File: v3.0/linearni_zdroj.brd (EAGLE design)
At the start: 160 x 100 mm, 29 parts, among them IC1 LM358N, IC2 LM358N, Q1 TIP120, Q2 TIP120

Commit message: zpřehlednění schématu
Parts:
- removed C1: 470u, rcl:E3,5-8
- removed R3: (no value), rcl:R0805
- removed ZD2: (no value), devices:DO34-5
- added ZD1, ZD3, ZD4: (no value), devices:MINIMELF
- moved R1 258.6 mm to (45.7, 57.1)
- moved R7 248.3 mm to (34.3, 30.5)
- moved R2 236.4 mm to (63.5, 36.8)
- moved C9 189.5 mm to (21.6, 55.9)
- moved C8 185.7 mm to (16.5, 58.4)
- moved R10 75.9 mm to (12.7, 53.3)
- moved IC2 75.5 mm to (11.4, 33.0)
- moved U$5 74.1 mm to (19.1, 43.2)
- moved R9 65.7 mm to (36.8, 41.9)
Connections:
- net A1: now also ZD1.C
- net A3: now also ZD4.C; no longer ZD2.C
- net GND: now also ZD1.A, ZD3.A, ZD4.A; no longer C1.-, R3.1, ZD2.A
- net N$11: now also ZD3.C
- net N$13: no longer C1.+, R3.2

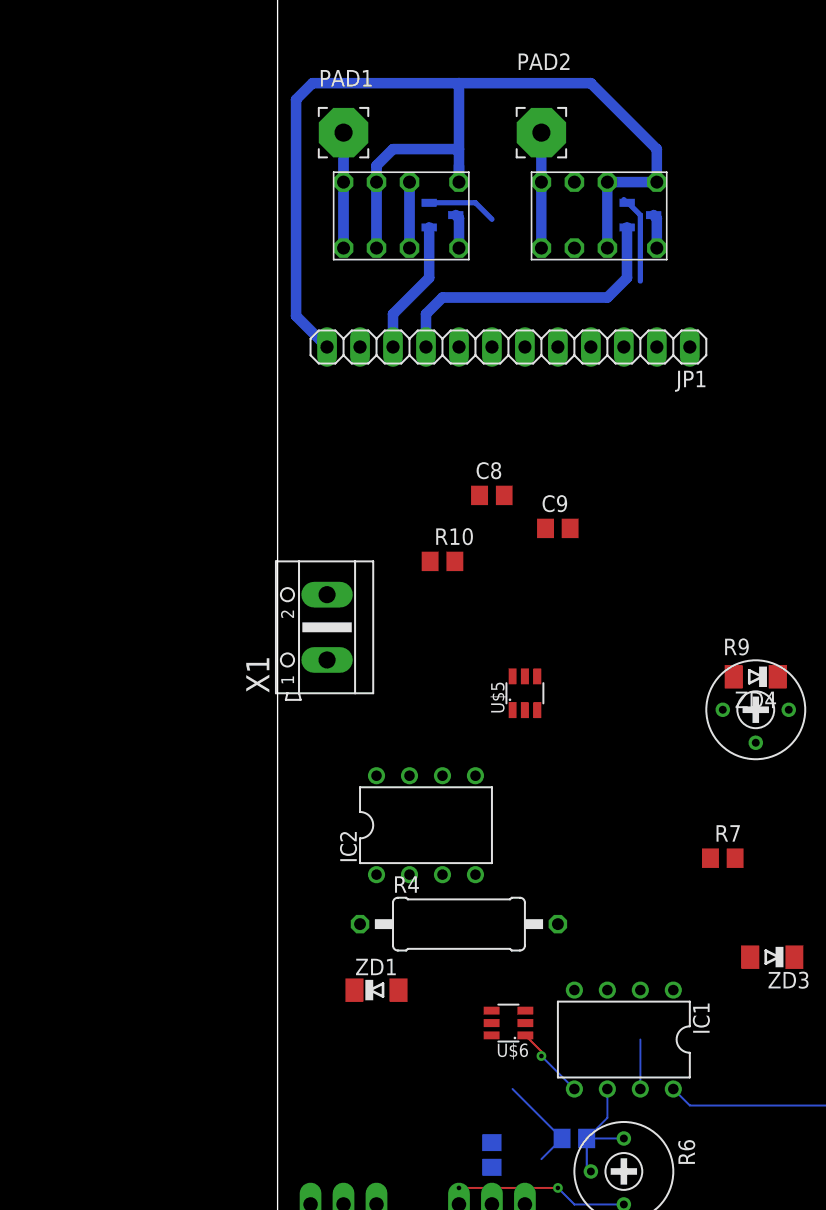
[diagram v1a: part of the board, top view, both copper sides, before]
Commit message: přidány pull-up rezistory I2C
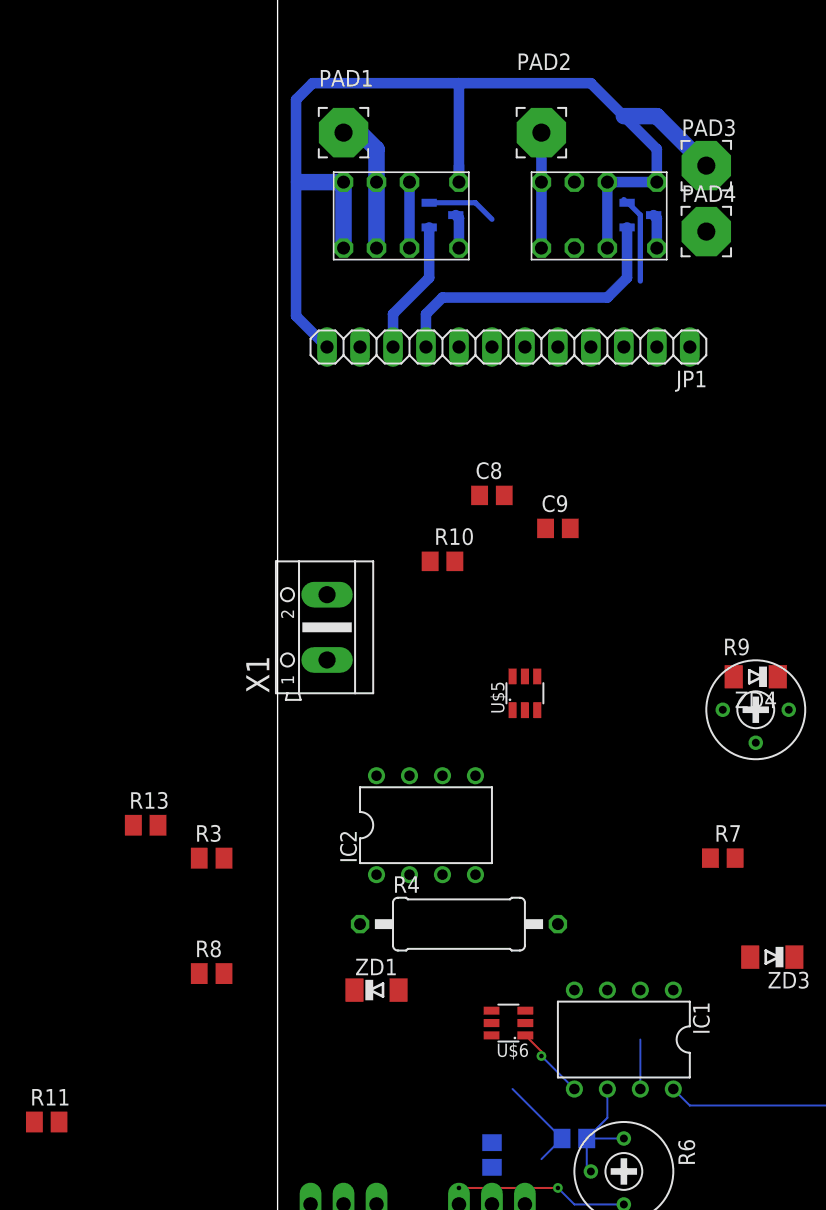
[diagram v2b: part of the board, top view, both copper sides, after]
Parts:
- added PAD3, PAD4: (no value), wirepad:3,81/1,4
- added R11, R13, R3, R8: (no value), rcl_my:M0805
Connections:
- net +24V: now also PAD3.1, U$2.8, U$2.9; no longer U$2.11, U$2.6
- net +3V3: now also R11.2, R13.2, R3.2, R8.2
- net GND: now also PAD4.1
- net N$10: now also U$2.11, U$2.6; no longer U$2.8, U$2.9
- net SCL: now also R13.1
- net SCL2: now also R8.1
- net SDA: now also R3.1
- net SDA2: now also R11.1
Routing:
- net +24V: track 84.0 -> 87.2 mm
- net N$10: track 8.89 -> 10.7 mm
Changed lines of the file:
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@@
 <attribute name="VALUE" x="38.481" y="46.863" size="1.27" layer="27" rot="R180"/>
+</element>
+<element name="PAD3" library="wirepad" library_urn="urn:adsk.eagle:library:412" package="3,81/1,4" package3d_urn="urn:adsk.eagle:package:30835/1" value="" x="33.02" y="83.82" smashed="yes">
+<attribute name="NAME" x="31.115" y="86.106" size="1.27" layer="25" ratio="10"/>
+<attribute name="POPULARITY" value="14" x="33.02" y="83.82" size="1.778" layer="27" display="off"/>
+<attribute name="VALUE" x="33.02" y="85.02" size="0.0254" layer="27"/>
+</element>
+<element name="PAD4" library="wirepad" library_urn="urn:adsk.eagle:library:412" package="3,81/1,4" package3d_urn="urn:adsk.eagle:package:30835/1" value="" x="33.02" y="78.74" smashed="yes">
+<attribute name="NAME" x="31.115" y="81.026" size="1.27" layer="25" ratio="10"/>
+<attribute name="POPULARITY" value="14" x="33.02" y="78.74" size="1.778" layer="27" display="off"/>
+<attribute name="VALUE" x="33.02" y="79.94" size="0.0254" layer="27"/>
+</element>
+<element name="R3" library="rcl_my" package="M0805" value="" x="-5.08" y="30.48" smashed="yes">
+<attribute name="NAME" x="-6.35" y="31.75" size="1.27" layer="25"/>
+<attribute name="VALUE" x="-6.35" y="27.94" size="1.27" layer="27"/>
+</element>
+<element name="R8" library="rcl_my" package="M0805" value="" x="-5.08" y="21.59" smashed="yes">
+<attribute name="NAME" x="-6.35" y="22.86" size="1.27" layer="25"/>
+<attribute name="VALUE" x="-6.35" y="19.05" size="1.27" layer="27"/>
+</element>
+<element name="R11" library="rcl_my" package="M0805" value="" x="-17.78" y="10.16" smashed="yes">
+<attribute name="NAME" x="-19.05" y="11.43" size="1.27" layer="25"/>
+<attribute name="VALUE" x="-19.05" y="7.62" size="1.27" layer="27"/>
+</element>
+<element name="R13" library="rcl_my" package="M0805" value="" x="-10.16" y="33.02" smashed="yes">
+<attribute name="NAME" x="-11.43" y="34.29" size="1.27" layer="25"/>
+<attribute name="VALUE" x="-11.43" y="30.48" size="1.27" layer="27"/>
 </element>
 </elements>
@@
 <contactref element="ZD1" pad="A"/>
 <contactref element="ZD3" pad="A"/>
+<contactref element="PAD4" pad="1"/>
 <wire x1="16.51" y1="79.69" x2="26.67" y2="81.2053" width="0" layer="19" extent="16-16"/>
 <wire x1="6.35" y1="69.85" x2="11.6753" y2="80.96" width="0" layer="19" extent="16-16"/>
@@
 <wire x1="35.13" y1="44.45" x2="19.05" y2="41.88" width="0" layer="19" extent="1-1"/>
 <wire x1="44.77" y1="57.15" x2="35.13" y2="44.45" width="0" layer="19" extent="1-1"/>
+<wire x1="33.02" y1="78.74" x2="20.32" y2="7.3" width="0" layer="19" extent="16-16"/>
 </signal>
 <signal name="VCC/2">
@@
 <contactref element="U$5" pad="5"/>
 <contactref element="JP1" pad="8"/>
+<contactref element="R13" pad="1"/>
 <wire x1="19.05" y1="44.48" x2="13.97" y2="69.85" width="0" layer="19" extent="1-1"/>
+<wire x1="-11.11" y1="33.02" x2="19.05" y2="44.48" width="0" layer="19" extent="1-1"/>
 </signal>
 <signal name="SDA">
 <contactref element="U$5" pad="4"/>
 <contactref element="JP1" pad="7"/>
+<contactref element="R3" pad="1"/>
 <wire x1="20" y1="44.48" x2="16.51" y2="69.85" width="0" layer="19" extent="1-1"/>
+<wire x1="-6.03" y1="30.48" x2="20" y2="44.48" width="0" layer="19" extent="1-1"/>
 </signal>
 <signal name="N$9">
@@
 <wire x1="5.08" y1="3.81" x2="10.16" y2="77.47" width="0" layer="19" extent="1-1"/>
 </signal>
-<signal name="N$10">
-<contactref element="PAD1" pad="1"/>
-<contactref element="U$2" pad="8"/>
-<wire x1="5.08" y1="86.36" x2="5.08" y2="82.55" width="0.8128" layer="16"/>
-<contactref element="U$2" pad="9"/>
-<wire x1="5.08" y1="77.47" x2="5.08" y2="82.55" width="0.8128" layer="16"/>
-</signal>
 <signal name="+24V">
-<contactref element="U$2" pad="6"/>
 <contactref element="U$1" pad="1"/>
 <contactref element="U$2" pad="1"/>
-<wire x1="7.62" y1="82.55" x2="7.62" y2="83.82" width="0.8128" layer="16"/>
-<wire x1="7.62" y1="83.82" x2="8.89" y2="85.09" width="0.8128" layer="16"/>
-<wire x1="8.89" y1="85.09" x2="13.97" y2="85.09" width="0.8128" layer="16"/>
 <wire x1="13.97" y1="83.82" x2="13.97" y2="82.55" width="0.8128" layer="16"/>
-<contactref element="U$2" pad="11"/>
 <contactref element="U$1" pad="4"/>
 <contactref element="U$1" pad="13"/>
 <wire x1="25.4" y1="77.47" x2="25.4" y2="82.55" width="0.8128" layer="16"/>
-<wire x1="7.62" y1="77.47" x2="7.62" y2="82.55" width="0.8128" layer="16"/>
-<wire x1="29.21" y1="85.09" x2="24.13" y2="90.17" width="0.8128" layer="16"/>
+<wire x1="29.21" y1="85.09" x2="26.67" y2="87.63" width="0.8128" layer="16"/>
+<wire x1="26.67" y1="87.63" x2="24.13" y2="90.17" width="0.8128" layer="16"/>
 <wire x1="24.13" y1="90.17" x2="13.97" y2="90.17" width="0.8128" layer="16"/>
-<wire x1="13.97" y1="85.09" x2="13.97" y2="82.55" width="0.8128" layer="16"/>
 <wire x1="29.21" y1="82.55" x2="29.21" y2="85.09" width="0.8128" layer="16"/>
 <wire x1="25.4" y1="82.55" x2="29.21" y2="82.55" width="0.8128" layer="16"/>
@@
 <wire x1="1.4224" y1="88.9" x2="2.6924" y2="90.17" width="0.8128" layer="16"/>
 <wire x1="2.6924" y1="90.17" x2="13.97" y2="90.17" width="0.8128" layer="16"/>
-<wire x1="13.97" y1="85.09" x2="13.97" y2="90.17" width="0.8128" layer="16"/>
+<wire x1="13.97" y1="82.55" x2="13.97" y2="90.17" width="0.8128" layer="16"/>
+<contactref element="U$2" pad="8"/>
+<contactref element="U$2" pad="9"/>
+<wire x1="5.08" y1="77.47" x2="5.08" y2="82.55" width="1.27" layer="16"/>
+<wire x1="5.08" y1="82.55" x2="1.651" y2="82.55" width="1.27" layer="16"/>
+<contactref element="PAD3" pad="1"/>
+<wire x1="33.02" y1="83.82" x2="29.21" y2="87.63" width="1.27" layer="16"/>
+<wire x1="29.21" y1="87.63" x2="26.67" y2="87.63" width="1.27" layer="16"/>
+<wire x1="3.81" y1="69.85" x2="5.08" y2="77.47" width="0" layer="19" extent="1-1"/>
 </signal>
 <signal name="N$16">
@@
 <contactref element="U$6" pad="6"/>
 <contactref element="JP1" pad="1"/>
-<wire x1="19.08" y1="18.73" x2="31.75" y2="69.85" width="0" layer="19" extent="1-1"/>
+<contactref element="R11" pad="2"/>
+<contactref element="R8" pad="2"/>
+<contactref element="R13" pad="2"/>
+<contactref element="R3" pad="2"/>
+<wire x1="18.1" y1="44.48" x2="31.75" y2="69.85" width="0" layer="19" extent="1-1"/>
+<wire x1="20" y1="41.88" x2="18.1" y2="44.48" width="0" layer="19" extent="1-1"/>
+<wire x1="19.08" y1="18.73" x2="20" y2="41.88" width="0" layer="19" extent="1-1"/>
 <wire x1="16.48" y1="16.83" x2="19.08" y2="18.73" width="0" layer="19" extent="1-1"/>
-<wire x1="18.1" y1="44.48" x2="16.48" y2="16.83" width="0" layer="19" extent="1-1"/>
-<wire x1="20" y1="41.88" x2="18.1" y2="44.48" width="0" layer="19" extent="1-1"/>
+<wire x1="-4.13" y1="30.48" x2="16.48" y2="16.83" width="0" layer="19" extent="1-1"/>
+<wire x1="-4.13" y1="21.59" x2="-4.13" y2="30.48" width="0" layer="19" extent="1-1"/>
+<wire x1="-16.83" y1="10.16" x2="-4.13" y2="21.59" width="0" layer="19" extent="1-1"/>
+<wire x1="-9.21" y1="33.02" x2="-16.83" y2="10.16" width="0" layer="19" extent="1-1"/>
 </signal>
 <signal name="SCL2">
 <contactref element="U$6" pad="5"/>
 <contactref element="JP1" pad="3"/>
+<contactref element="R8" pad="1"/>
 <wire x1="16.48" y1="17.78" x2="26.67" y2="69.85" width="0" layer="19" extent="1-1"/>
+<wire x1="-6.03" y1="21.59" x2="16.48" y2="17.78" width="0" layer="19" extent="1-1"/>
 </signal>
 <signal name="SDA2">
 <contactref element="U$6" pad="4"/>
 <contactref element="JP1" pad="2"/>
+<contactref element="R11" pad="1"/>
 <wire x1="16.48" y1="18.73" x2="29.21" y2="69.85" width="0" layer="19" extent="1-1"/>
+<wire x1="-18.73" y1="10.16" x2="16.48" y2="18.73" width="0" layer="19" extent="1-1"/>
 </signal>
 <signal name="N$14">
@@
 <wire x1="11.6753" y1="75.1753" x2="8.89" y2="72.39" width="0.8128" layer="16"/>
 </signal>
+<signal name="N$10">
+<contactref element="U$2" pad="6"/>
+<contactref element="U$2" pad="11"/>
+<contactref element="PAD1" pad="1"/>
+<wire x1="7.62" y1="77.47" x2="7.62" y2="82.55" width="1.27" layer="16"/>
+<wire x1="5.08" y1="86.36" x2="6.35" y2="86.36" width="1.27" layer="16"/>
+<wire x1="6.35" y1="86.36" x2="7.62" y2="85.09" width="1.27" layer="16"/>
+<wire x1="7.62" y1="85.09" x2="7.62" y2="82.55" width="1.27" layer="16"/>
+</signal>
 </signals>

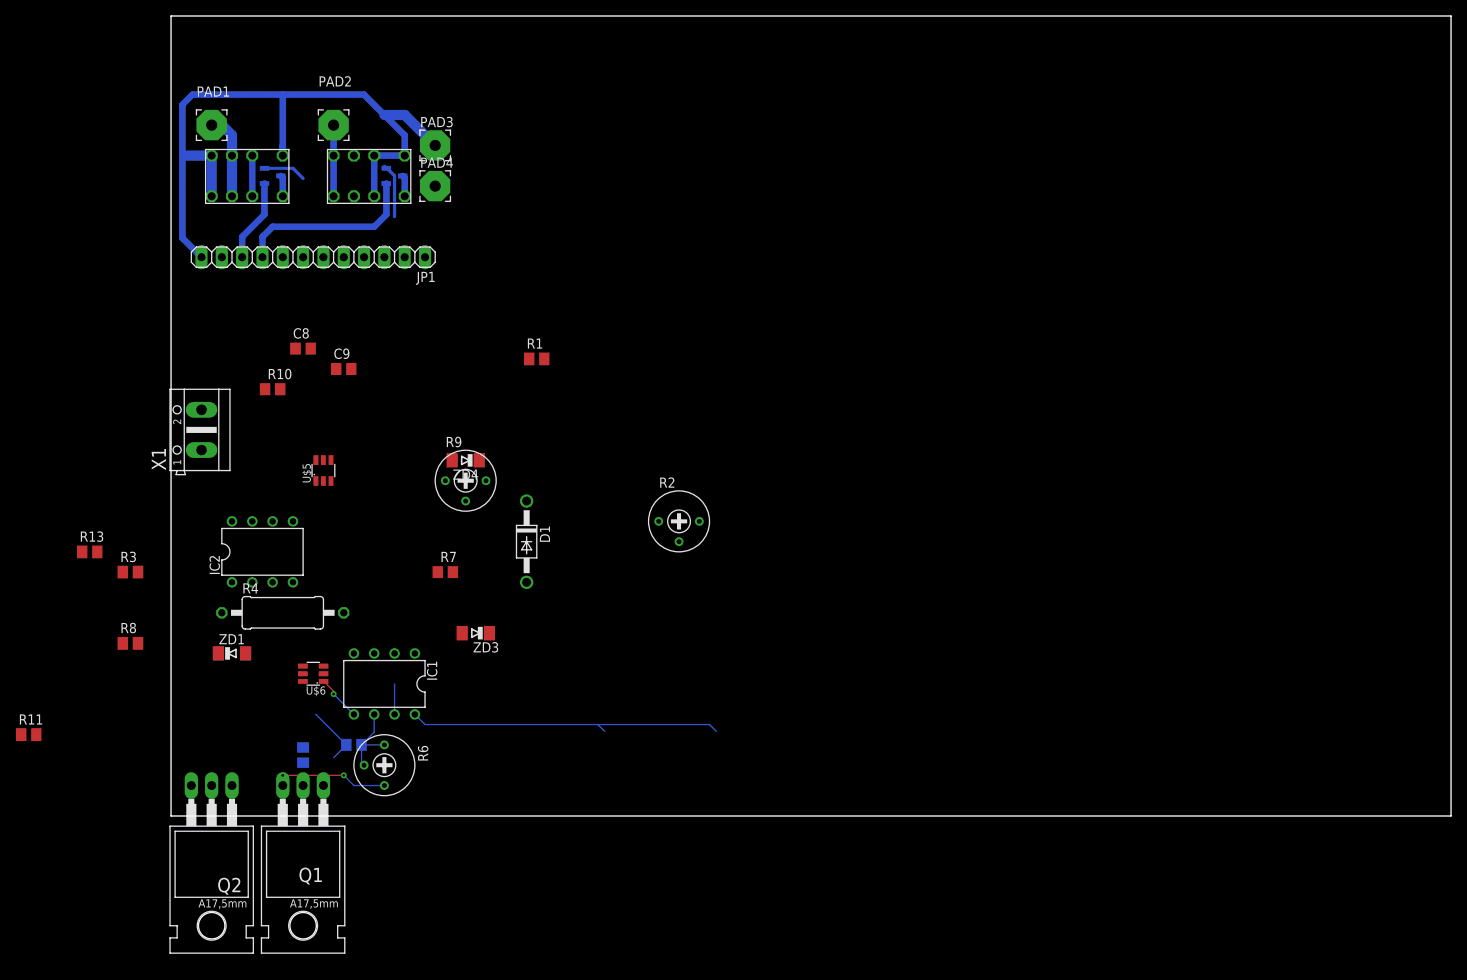
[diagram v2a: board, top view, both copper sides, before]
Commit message: deska lineárního regulátoru
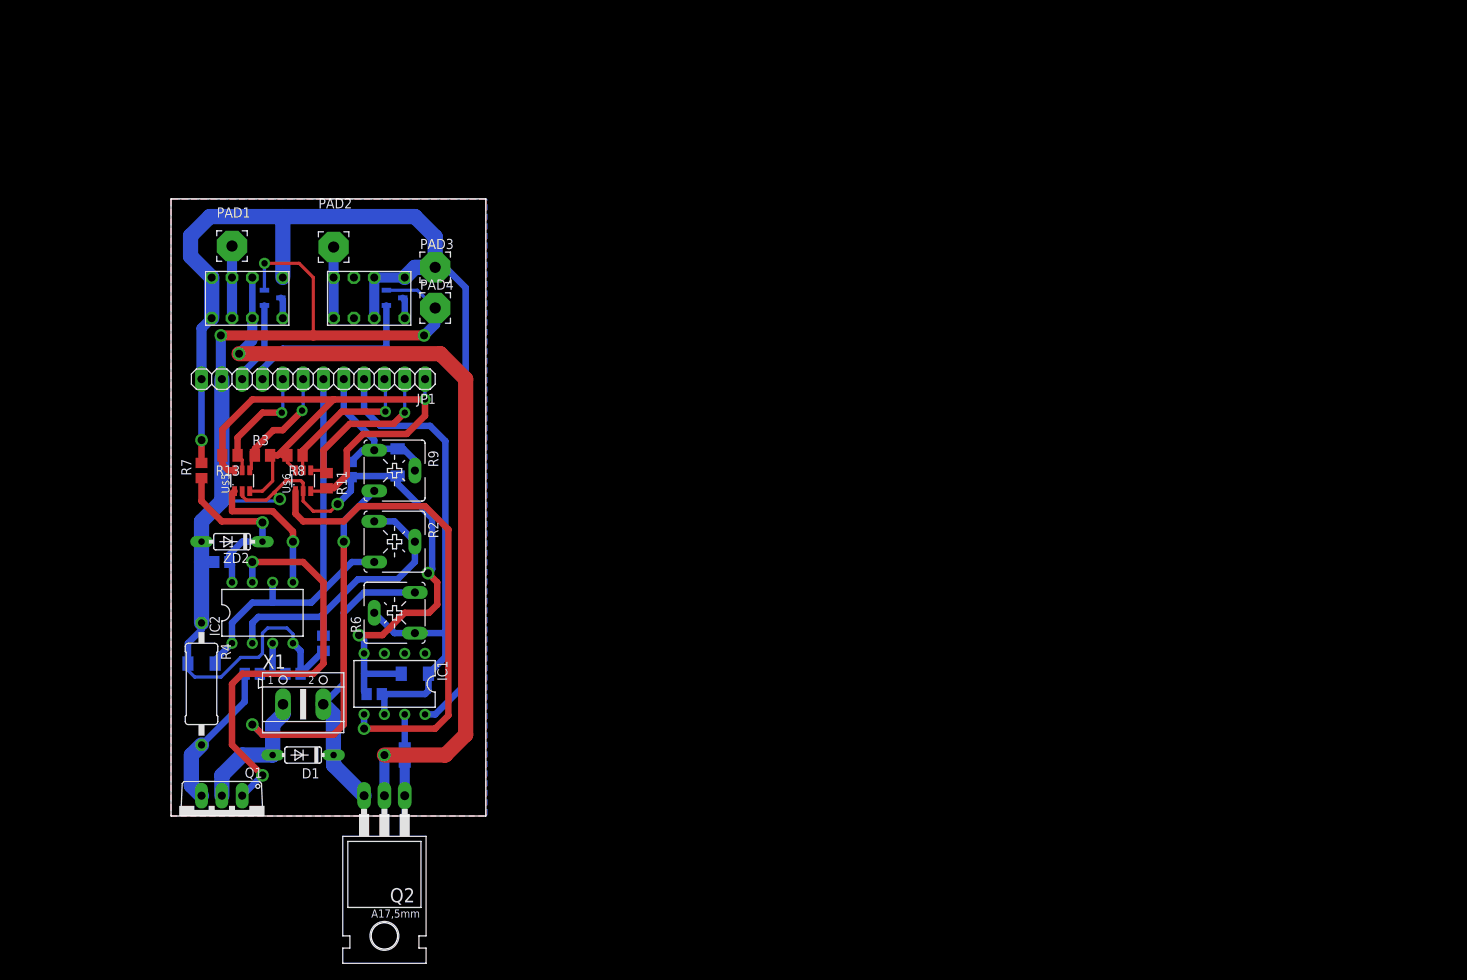
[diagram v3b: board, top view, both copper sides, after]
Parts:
- removed C8: (no value), rcl:C0805
- added C1: (no value), rcl:C0805
- added R14: (no value), rcl:R0805
- added ZD2: (no value), devices:DO35Z7
- D1: value 1N4004 -> (none); device diode:DO41-10 -> devices:DO35-7B
- Q1: value TIP120 -> IRFZ34NAV; device transistor-power:TO220AH -> devices:TO220AV
- R2, R6, R9: device rcl:RTRIM3339P -> pot:CA6V
- moved R11 48.9 mm to (19.4, 41.9), turned to 270 degrees
- moved R1 44.5 mm to (19.1, 21.6), flipped to the bottom, turned to 90 degrees
- moved D1 38.6 mm to (16.5, 7.62), turned to 180 degrees
- moved X1 36.6 mm to (16.5, 14.0), turned to 0 degrees
- moved R2 35.7 mm to (27.9, 34.3), turned to 270 degrees
- moved R7 33.0 mm to (3.81, 43.2), turned to 90 degrees
- moved R8 31.2 mm to (15.5, 45.1), turned to 180 degrees
- moved C9 28.5 mm to (6.35, 31.8), flipped to the bottom
- moved U$6 24.2 mm to (16.5, 41.9), turned to 0 degrees
- moved R3 22.0 mm to (11.4, 45.1)
- moved Q2 21.6 mm to (26.7, -3.81)
- moved R13 21.3 mm to (7.37, 45.1), turned to 180 degrees
- moved R6 19.1 mm to (27.9, 25.4), turned to 90 degrees
- moved PAD1 15.3 mm to (7.62, 71.2)
- moved U$1 15.2 mm to (25.4, 64.8)
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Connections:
- removed net A1: IC1.2, IC2.1, R2.3, ZD1.C
- removed net A3: R10.2, R9.1, R9.2, ZD4.C
- removed net N$11: IC1.6, R5.2, R6.1, R6.2, ZD3.C
- removed net N$14: JP1.4
- removed net N$15: JP1.5
- removed net N$18: JP1.6
- removed net VCC/2: C8.1, C9.1, IC1.8, IC2.8
- new net ADC0: IC2.1, IC2.6, JP1.6, R2.E, ZD1.C
- new net ADC1: JP1.5, R10.2, R9.A, R9.S, ZD4.C
- new net ADC2: IC1.6, JP1.4, R5.2, R6.A, R6.S, ZD3.C
- new net N$20: C1.1, IC2.3, R14.1
- net +24V: now also IC1.8, R7.2
- net GND: now also C1.2, ZD2.A; no longer C8.2
- net N$1: now also Q1.S, R14.2; no longer IC2.3, Q1.E
- net N$13: now also R6.E; no longer R6.3
- net N$2: now also IC2.7, Q1.G; no longer IC1.1, R7.2
- net N$3: now also R2.A, R2.S; no longer R2.1, R2.2
- net N$5: now also C9.1, IC2.8, ZD2.C; no longer Q1.B
- net N$6: now also IC2.5; no longer IC1.3
- net N$7: now also Q1.D, R9.E; no longer Q1.C, R9.3
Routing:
- net GND: track 19.8 -> 206.7 mm, vias 0 -> 7
- net N$8: track 5.08 -> 100.6 mm, vias 0 -> 2
- net +3V3: track 0.00 -> 79.6 mm, vias 0 -> 1
- net ADC2: track 0.00 -> 66.3 mm
- net N$7: track 0.00 -> 63.2 mm, vias 0 -> 2
- net +24V: track 87.2 -> 148.3 mm, vias 0 -> 1
- net ADC0: track 0.00 -> 55.8 mm
- net N$9: track 5.70 -> 60.6 mm
- net N$2: track 0.00 -> 51.7 mm, vias 0 -> 2
- net VCC/2: track 39.8 -> 0.00 mm
- net N$3: track 0.00 -> 37.4 mm
- net N$13: track 13.2 -> 36.0 mm, vias 2 -> 0
- net N$5: track 0.00 -> 22.4 mm, vias 0 -> 1
- net SDA2: track 0.00 -> 21.4 mm, vias 0 -> 1
- net ADC1: track 0.00 -> 21.0 mm
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- added copper zone on layer 1, net GND
- added copper zone on layer 16, net GND
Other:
- board size 160 x 100 mm -> 39.4 x 77.1 mm
